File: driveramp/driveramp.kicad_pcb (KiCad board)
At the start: 2 copper layers, 109 x 79 mm, 88 parts, among them J1 SMA, J2 SMA, K1 CONN_3, P2 CONN_2, Q1 BC547BTA, T1 MABACT0067, T2 2x Fair-Rite 2843006802, coax, U1 DG9411, U2 MRFE6VP100H, U3 LM317HV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

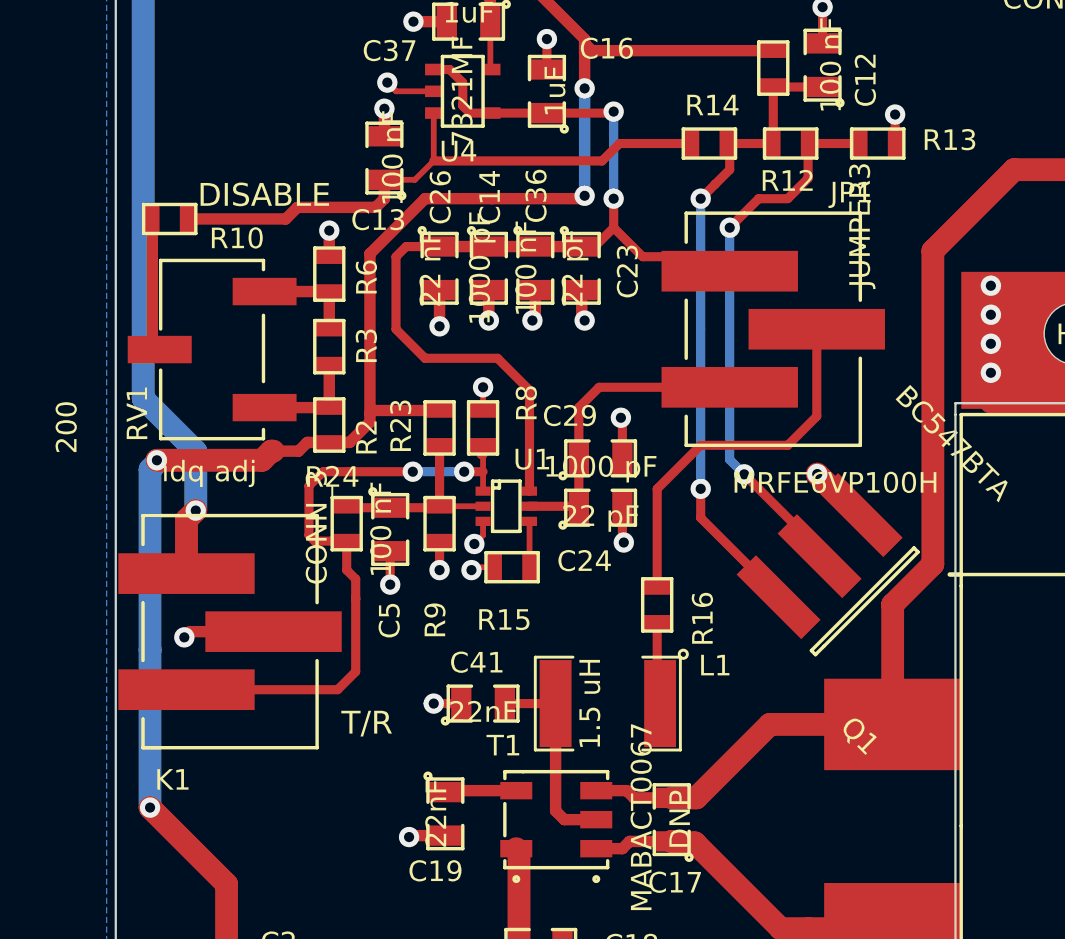
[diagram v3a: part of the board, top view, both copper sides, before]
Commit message: changed all 3 pin headers to molex smd connectors available in tube packaging..
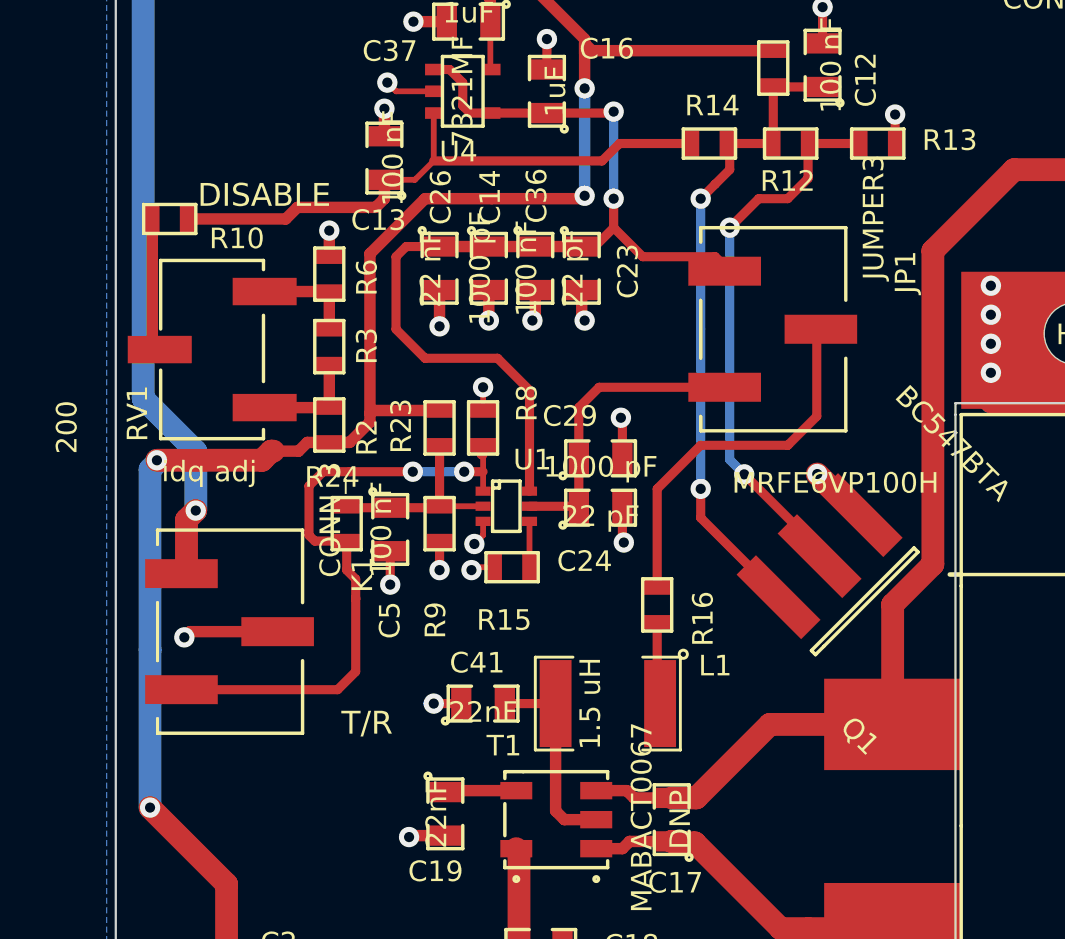
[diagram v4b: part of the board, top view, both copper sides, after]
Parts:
- JP1, K1: footprint localconn:3-647166-3 -> sdtransmitter:0740991003
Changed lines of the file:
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@@
   )
   (setup
-    (last_trace_width 0.4)
+    (last_trace_width 0.254)
     (user_trace_width 0.4)
     (user_trace_width 0.5)
@@
     (mod_text_size 0.9 0.9)
     (mod_text_width 0.225)
-    (pad_size 3.6576 2.032)
+    (pad_size 1.27 3.18)
     (pad_drill 0)
     (pad_to_mask_clearance 0)
@@
     )
   )
-  (module localconn:3-647166-3 (layer F.Cu)
-    (at 81 101.5 270)
-    (fp_text reference K1 (at 6.5 2.5 360) (layer F.SilkS)
-      (effects (font (size 0.9 0.9) (thickness 0.225)))
-    )
-    (fp_text value CONN_3 (at -4.572 -3.81 270) (layer F.SilkS)
-      (effects (font (size 0.9 0.9) (thickness 0.225)))
-    )
-    (fp_line (start -1.27 -3.81) (end -5.08 -3.81) (layer F.SilkS) (width 0.15))
-    (fp_line (start -5.08 -3.81) (end -5.08 1.27) (layer F.SilkS) (width 0.15))
-    (fp_line (start 3.81 3.81) (end 5.08 3.81) (layer F.SilkS) (width 0.15))
-    (fp_line (start 5.08 3.81) (end 5.08 -3.81) (layer F.SilkS) (width 0.15))
-    (fp_line (start 5.08 -3.81) (end 1.27 -3.81) (layer F.SilkS) (width 0.15))
-    (fp_line (start -1.27 3.81) (end 1.27 3.81) (layer F.SilkS) (width 0.15))
-    (fp_line (start -5.08 1.27) (end -5.08 3.81) (layer F.SilkS) (width 0.15))
-    (fp_line (start -5.08 3.81) (end -3.81 3.81) (layer F.SilkS) (width 0.15))
-    (pad 1 smd rect (at -2.54 1.905 270) (size 1.78 5.97) (layers F.Cu F.Paste F.Mask)
-      (net 38 VPP))
-    (pad 2 smd rect (at 0 -1.905 270) (size 1.78 5.97) (layers F.Cu F.Paste F.Mask)
-      (net 1 GND))
-    (pad 3 smd rect (at 2.54 1.905 270) (size 1.78 5.97) (layers F.Cu F.Paste F.Mask)
-      (net 34 "Net-(K1-Pad3)"))
-  )
   (module SMD_Packages:SMD-0603 (layer F.Cu)
     (at 85.344 85.852 90)
@@
       (solder_mask_margin 2))
   )
-  (module localconn:3-647166-3 (layer F.Cu)
-    (at 104.775 88.265 270)
-    (fp_text reference JP1 (at -5.969 -3.429 360) (layer F.SilkS)
-      (effects (font (size 0.9 0.9) (thickness 0.225)))
-    )
-    (fp_text value JUMPER3 (at -4.572 -3.81 270) (layer F.SilkS)
-      (effects (font (size 0.9 0.9) (thickness 0.225)))
-    )
-    (fp_line (start -1.27 -3.81) (end -5.08 -3.81) (layer F.SilkS) (width 0.15))
-    (fp_line (start -5.08 -3.81) (end -5.08 1.27) (layer F.SilkS) (width 0.15))
-    (fp_line (start 3.81 3.81) (end 5.08 3.81) (layer F.SilkS) (width 0.15))
-    (fp_line (start 5.08 3.81) (end 5.08 -3.81) (layer F.SilkS) (width 0.15))
-    (fp_line (start 5.08 -3.81) (end 1.27 -3.81) (layer F.SilkS) (width 0.15))
-    (fp_line (start -1.27 3.81) (end 1.27 3.81) (layer F.SilkS) (width 0.15))
-    (fp_line (start -5.08 1.27) (end -5.08 3.81) (layer F.SilkS) (width 0.15))
-    (fp_line (start -5.08 3.81) (end -3.81 3.81) (layer F.SilkS) (width 0.15))
-    (pad 1 smd rect (at -2.54 1.905 270) (size 1.78 5.97) (layers F.Cu F.Paste F.Mask)
-      (net 24 "Net-(C14-Pad1)"))
-    (pad 2 smd rect (at 0 -1.905 270) (size 1.78 5.97) (layers F.Cu F.Paste F.Mask)
-      (net 39 "Net-(JP1-Pad2)"))
-    (pad 3 smd rect (at 2.54 1.905 270) (size 1.78 5.97) (layers F.Cu F.Paste F.Mask)
-      (net 32 "Net-(C24-Pad1)"))
-  )
   (module SMD_Packages:SMD-1812 (layer F.Cu)
     (at 93.2 120.6)
@@
     )
   )
+  (module sdtransmitter:0740991003 (layer F.Cu)
+    (at 104.775 88.265 270)
+    (fp_text reference JP1 (at -2.5 -5.8 270) (layer F.SilkS)
+      (effects (font (size 0.9 0.9) (thickness 0.225)))
+    )
+    (fp_text value JUMPER3 (at -4.9 -4.4 270) (layer F.SilkS)
+      (effects (font (size 0.9 0.9) (thickness 0.225)))
+    )
+    (fp_line (start -1.27 3.175) (end 1.27 3.175) (layer F.SilkS) (width 0.15))
+    (fp_line (start -4.445 -3.175) (end -1.27 -3.175) (layer F.SilkS) (width 0.15))
+    (fp_line (start -3.81 3.175) (end -4.445 3.175) (layer F.SilkS) (width 0.15))
+    (fp_line (start -4.445 3.175) (end -4.445 -3.175) (layer F.SilkS) (width 0.15))
+    (fp_line (start 1.27 -3.175) (end 4.445 -3.175) (layer F.SilkS) (width 0.15))
+    (fp_line (start 4.445 -3.175) (end 4.445 3.175) (layer F.SilkS) (width 0.15))
+    (fp_line (start 4.445 3.175) (end 3.81 3.175) (layer F.SilkS) (width 0.15))
+    (pad 1 smd rect (at -2.54 2.127 270) (size 1.27 3.18) (layers F.Cu F.Paste F.Mask)
+      (net 24 "Net-(C14-Pad1)"))
+    (pad 2 smd rect (at 0 -2.083 270) (size 1.27 3.18) (layers F.Cu F.Paste F.Mask)
+      (net 39 "Net-(JP1-Pad2)"))
+    (pad 3 smd rect (at 2.54 2.127 270) (size 1.27 3.18) (layers F.Cu F.Paste F.Mask)
+      (net 32 "Net-(C24-Pad1)"))
+  )
+  (module sdtransmitter:0740991003 (layer F.Cu)
+    (at 81 101.5 270)
+    (fp_text reference K1 (at -2.5 -5.8 270) (layer F.SilkS)
+      (effects (font (size 0.9 0.9) (thickness 0.225)))
+    )
+    (fp_text value CONN_3 (at -4.9 -4.4 270) (layer F.SilkS)
+      (effects (font (size 0.9 0.9) (thickness 0.225)))
+    )
+    (fp_line (start -1.27 3.175) (end 1.27 3.175) (layer F.SilkS) (width 0.15))
+    (fp_line (start -4.445 -3.175) (end -1.27 -3.175) (layer F.SilkS) (width 0.15))
+    (fp_line (start -3.81 3.175) (end -4.445 3.175) (layer F.SilkS) (width 0.15))
+    (fp_line (start -4.445 3.175) (end -4.445 -3.175) (layer F.SilkS) (width 0.15))
+    (fp_line (start 1.27 -3.175) (end 4.445 -3.175) (layer F.SilkS) (width 0.15))
+    (fp_line (start 4.445 -3.175) (end 4.445 3.175) (layer F.SilkS) (width 0.15))
+    (fp_line (start 4.445 3.175) (end 3.81 3.175) (layer F.SilkS) (width 0.15))
+    (pad 1 smd rect (at -2.54 2.127 270) (size 1.27 3.18) (layers F.Cu F.Paste F.Mask)
+      (net 38 VPP))
+    (pad 2 smd rect (at 0 -2.083 270) (size 1.27 3.18) (layers F.Cu F.Paste F.Mask)
+      (net 1 GND))
+    (pad 3 smd rect (at 2.54 2.127 270) (size 1.27 3.18) (layers F.Cu F.Paste F.Mask)
+      (net 34 "Net-(K1-Pad3)"))
+  )
   (gr_line (start 123.25 128.5) (end 123.25 128) (angle 90) (layer Edge.Cuts) (width 0.1))
   (gr_line (start 112.75 128.5) (end 123.25 128.5) (angle 90) (layer Edge.Cuts) (width 0.1))
@@
   (via (at 134 85.4) (size 0.889) (layers F.Cu B.Cu) (net 0))
   (segment (start 134.4 85.8) (end 134 85.4) (width 1) (layer F.Cu) (net 0))
-  (segment (start 92.50018 125.4) (end 91.364 125.4) (width 0.4) (layer F.Cu) (net 1) (status C00000))
-  (segment (start 91.364 125.4) (end 90.932 124.968) (width 0.4) (layer F.Cu) (net 1) (status 400000))
-  (segment (start 94.3493 125.4) (end 92.50018 125.4) (width 0.4) (layer F.Cu) (net 1) (status C00000))
-  (segment (start 95.45166 125.4) (end 94.3493 125.4) (width 0.4) (layer F.Cu) (net 1) (status C00000))
+  (segment (start 92.50018 125.4) (end 91.364 125.4) (width 0.4) (layer F.Cu) (net 1))
+  (segment (start 91.364 125.4) (end 90.932 124.968) (width 0.4) (layer F.Cu) (net 1))
+  (segment (start 94.3493 125.4) (end 92.50018 125.4) (width 0.4) (layer F.Cu) (net 1))
+  (segment (start 95.45166 125.4) (end 94.3493 125.4) (width 0.4) (layer F.Cu) (net 1))
   (segment (start 150.876 94.234) (end 150.876 92.964) (width 1) (layer F.Cu) (net 1))
   (via (at 150.876 92.964) (size 0.889) (layers F.Cu B.Cu) (net 1))
@@
   (segment (start 89.916 104.648) (end 89.662 104.648) (width 0.4) (layer B.Cu) (net 1))
   (via (at 89.916 104.648) (size 0.889) (layers F.Cu B.Cu) (net 1))
-  (segment (start 82.905 101.5) (end 79.25 101.5) (width 0.5) (layer F.Cu) (net 1))
-  (via (at 79 101.75) (size 0.889) (layers F.Cu B.Cu) (net 1))
-  (segment (start 79.25 101.5) (end 79 101.75) (width 0.5) (layer F.Cu) (net 1))
   (segment (start 118 131.25) (end 116.4 131.25) (width 1) (layer F.Cu) (net 1))
   (segment (start 116.4 131.25) (end 114.3 133.35) (width 1) (layer F.Cu) (net 1))
@@
   (segment (start 151 110) (end 147.846 110) (width 2) (layer F.Cu) (net 1))
   (segment (start 147.828 109.982) (end 148.982 109.982) (width 0.254) (layer B.Cu) (net 1))
+  (segment (start 82.905 101.5) (end 79.25 101.5) (width 0.5) (layer F.Cu) (net 1))
+  (via (at 79 101.75) (size 0.889) (layers F.Cu B.Cu) (net 1))
+  (segment (start 79.25 101.5) (end 79 101.75) (width 0.5) (layer F.Cu) (net 1))
   (segment (start 100.33 108.7755) (end 101.4095 108.7755) (width 1) (layer F.Cu) (net 2))
   (segment (start 104.625 105.56) (end 110 105.56) (width 1) (layer F.Cu) (net 2))
@@
   (segment (start 96.2025 96.012) (end 96.266 96.0755) (width 0.4) (layer F.Cu) (net 32))
   (segment (start 96.266 96.0755) (end 96.266 93.9165) (width 0.4) (layer F.Cu) (net 32))
-  (segment (start 99.695 101.092) (end 99.695 104.521) (width 0.4) (layer F.Cu) (net 33) (status C00000))
-  (segment (start 99.695 104.521) (end 99.822 104.648) (width 0.4) (layer F.Cu) (net 33) (status C00000))
+  (segment (start 99.695 101.092) (end 99.695 104.521) (width 0.4) (layer F.Cu) (net 33))
+  (segment (start 99.695 104.521) (end 99.822 104.648) (width 0.4) (layer F.Cu) (net 33))
   (segment (start 92.075 94.5) (end 91.25 94.5) (width 0.4) (layer F.Cu) (net 34))
   (segment (start 91.25 94.5) (end 91.25 94.5) (width 0.4) (layer F.Cu) (net 34))

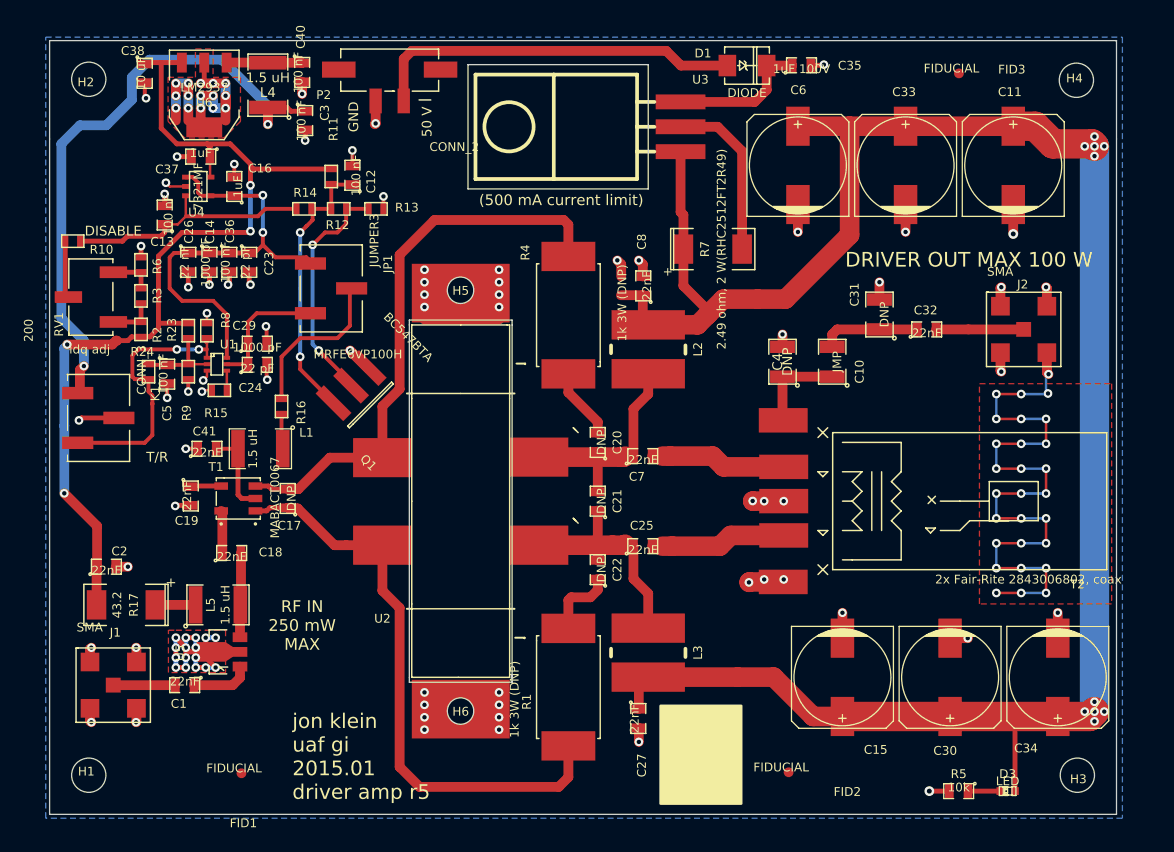
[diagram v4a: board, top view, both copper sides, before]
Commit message: rearranged high power T/R switch to place all connectors on one side for easier mounting to cases
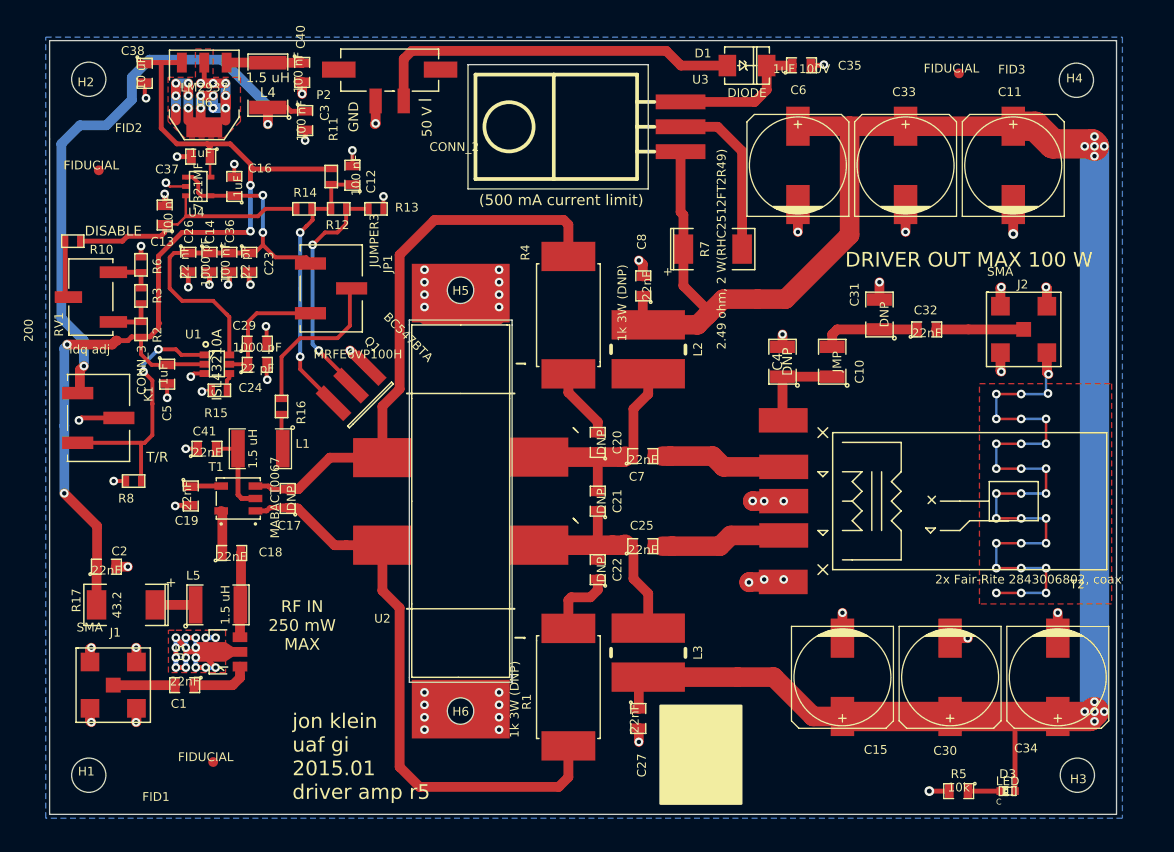
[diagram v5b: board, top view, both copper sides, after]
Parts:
- removed R23: 6.2 k, SMD_Packages:SMD-0603
- removed R24: DNP, SMD_Packages:SMD-0603
- removed R9: 9.1k, SMD_Packages:SMD-0603
- C5: value 100 nF -> 1uF
- U1: value DG9411 -> ISL43210A; footprint Transistors_SMD:sc70-6 -> SMD_Packages:SOT-23-6
- moved FID2 93.5 mm to (81.0, 76.2)
- moved R8 17.1 mm to (84.6, 108.0), turned to 0 degrees
- moved FID1 3.11 mm to (92.7, 136.7)
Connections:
- C5 pad 1: Net-(C5-Pad1) -> +8V
- U1 pad 2: Net-(C5-Pad1) -> +8V
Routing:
- net Net-(C5-Pad1): track 8.78 -> 0.00 mm
- net +8V: track 99.5 -> 105.4 mm
- net VDD: track 224.6 -> 222.4 mm
- net (no net): track 1.81 -> 0.00 mm, vias 1 -> 0
- net Net-(K1-Pad3): track 28.0 -> 26.6 mm
- net GND: track 264.3 -> 263.6 mm, vias 127 -> 126
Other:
- board text added: "C"

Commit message: changed 8v regulator on driver amp for fault shutdown
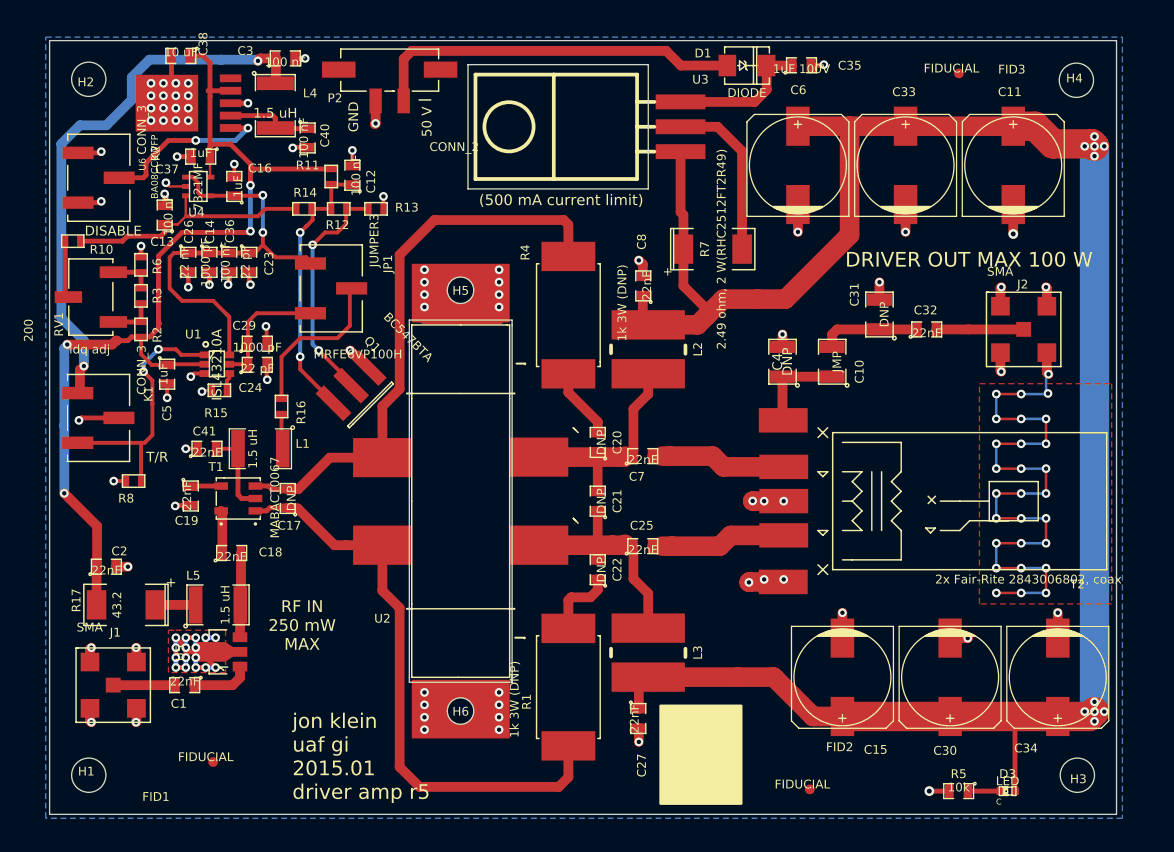
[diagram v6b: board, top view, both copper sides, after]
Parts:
- added K2: CONN_3, sdtransmitter:0740991003, F.Cu at (81.0, 77.0)
- U6: value LM2937 -> BA08CC0WFP; footprint SMD_Packages:SOT-223 -> to252_5:TO252-5
- moved FID2 96.3 mm to (153.7, 139.4)
- moved C40 6.72 mm to (102.4, 72.9)
- moved C3 6.67 mm to (100.1, 64.8), turned to 0 degrees
- moved C38 4.09 mm to (89.4, 64.5), turned to 180 degrees
- moved U6 2.82 mm to (94.5, 69.3), turned to 90 degrees
- moved L4 2.23 mm to (99.1, 69.6), turned to 270 degrees
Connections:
- U6 pad 1: Net-(C40-Pad1) -> /~FAULT
- U6 pad 2: GND -> Net-(C40-Pad1)
- U6 pad 3: +8V -> GND
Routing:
- net /~FAULT: track 0.00 -> 17.8 mm, vias 0 -> 2
- net GND: track 263.6 -> 271.9 mm, vias 126 -> 129
- net VPP: track 62.1 -> 56.3 mm
- net +8V: track 105.4 -> 102.3 mm
- net Net-(C40-Pad1): track 7.73 -> 9.02 mm
